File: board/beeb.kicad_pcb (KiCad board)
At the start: 2 copper layers, 24 parts, among them J2 AVR-JTAG-10, SW1 SW_DIP_x08, U2 ps2, U3 XC95144XL-TQ100, U4 beebKB, U5 OKI-78SR-3.3_1.5-W36-C

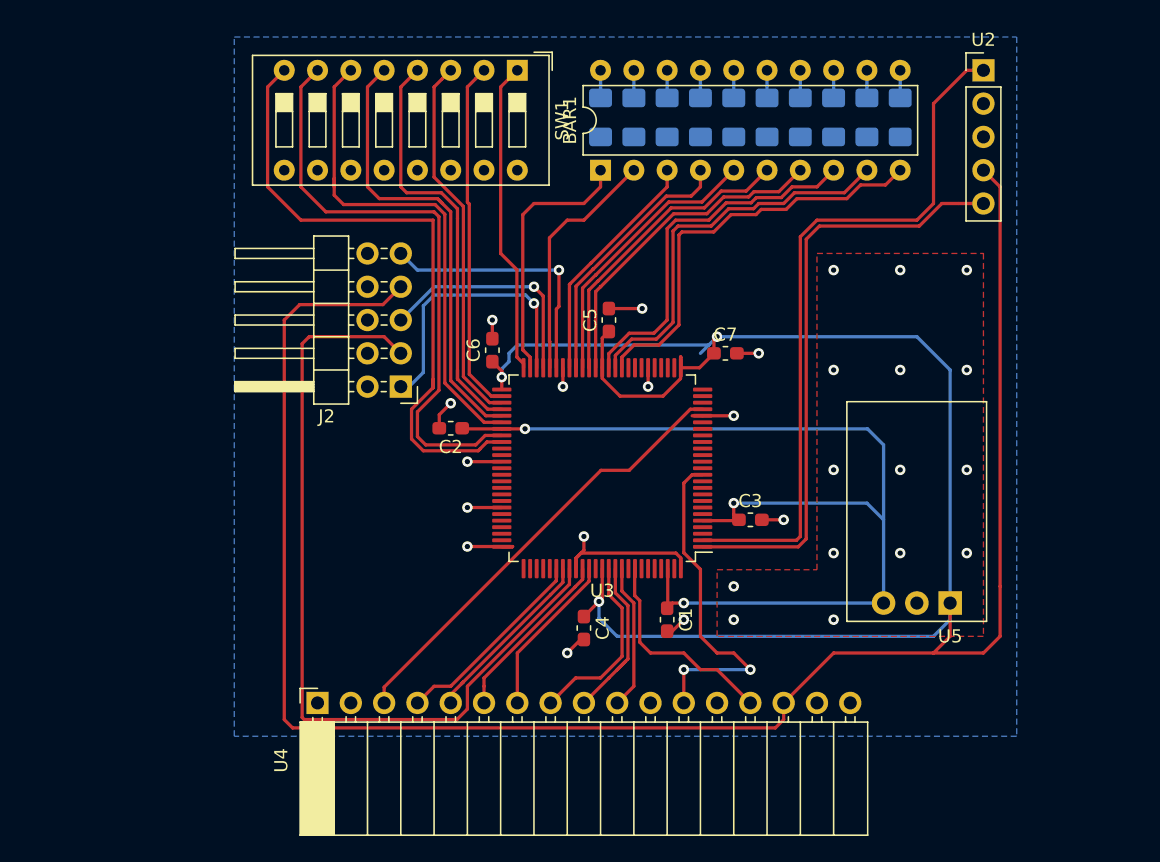
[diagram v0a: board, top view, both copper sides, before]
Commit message: Widen clearance around jtag vias
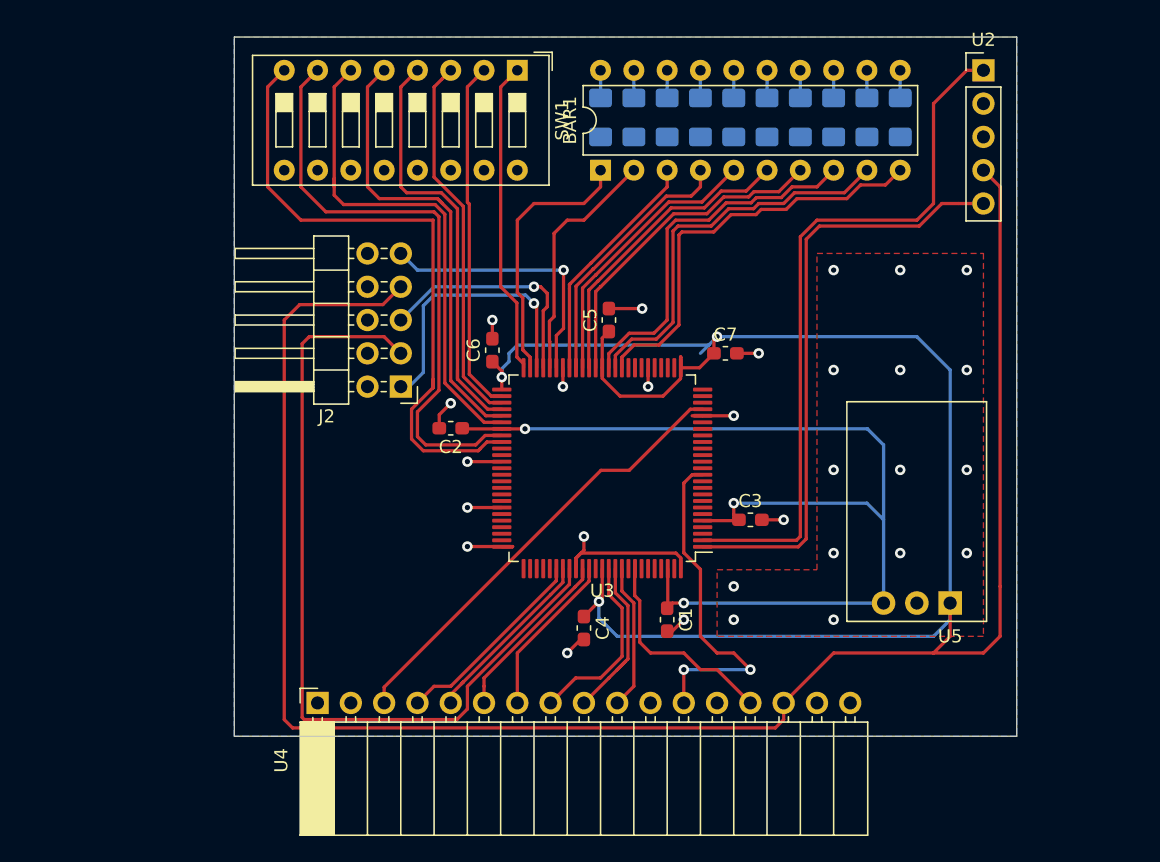
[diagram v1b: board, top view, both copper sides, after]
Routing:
- net /TMS: track 18.3 -> 18.9 mm
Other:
- board outline added: 59.7 x 53.3 mm
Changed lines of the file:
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@@
   (general
     (thickness 1.6)
-    (drawings 1)
-    (tracks 433)
+    (drawings 5)
+    (tracks 439)
     (zones 0)
     (modules 24)
@@
     (pad_to_mask_clearance 0.05)
     (aux_axis_origin 0 0)
+    (grid_origin 83.82 106.68)
     (visible_elements 7FFFFFFF)
     (pcbplotparams
@@
     )
   )
+  (gr_line (start 54.61 132.08) (end 54.61 78.74) (layer Edge.Cuts) (width 0.05))
+  (gr_line (start 114.3 132.08) (end 54.61 132.08) (layer Edge.Cuts) (width 0.05))
+  (gr_line (start 114.3 78.74) (end 114.3 132.08) (layer Edge.Cuts) (width 0.05))
+  (gr_line (start 54.61 78.74) (end 114.3 78.74) (layer Edge.Cuts) (width 0.05))
   (gr_poly (pts (xy 111.76 124.46) (xy 91.44 124.46) (xy 91.44 119.38) (xy 99.06 119.38) (xy 99.06 95.25) (xy 111.76 95.25)) (layer F.CrtYd) (width 0.1))
   (segment (start 82.55 81.28) (end 82.55 83.385) (width 0.25) (layer B.Cu) (net 1))
@@
   (via (at 110.49 118.11) (size 0.8) (drill 0.4) (layers F.Cu B.Cu) (net 11))
   (via (at 110.49 104.14) (size 0.8) (drill 0.4) (layers F.Cu B.Cu) (net 11))
-  (via (at 79.375 96.52) (size 0.8) (drill 0.4) (layers F.Cu B.Cu) (net 12))
-  (segment (start 79.375 99.299) (end 79.375 96.52) (width 0.25) (layer F.Cu) (net 12))
-  (segment (start 79.177 99.497) (end 79.375 99.299) (width 0.25) (layer F.Cu) (net 12))
-  (segment (start 79.177 103.9705) (end 79.177 99.497) (width 0.25) (layer F.Cu) (net 12))
+  (segment (start 79.177 103.9705) (end 79.177 101.51499) (width 0.25) (layer F.Cu) (net 12))
+  (segment (start 79.72699 100.965) (end 79.72699 96.52) (width 0.25) (layer F.Cu) (net 12))
+  (segment (start 79.177 101.51499) (end 79.72699 100.965) (width 0.25) (layer F.Cu) (net 12))
   (segment (start 68.58 96.52) (end 67.31 95.25) (width 0.25) (layer B.Cu) (net 12))
-  (segment (start 79.375 96.52) (end 68.58 96.52) (width 0.25) (layer B.Cu) (net 12))
+  (via (at 79.72699 96.52) (size 0.8) (drill 0.4) (layers F.Cu B.Cu) (net 12))
+  (segment (start 79.72699 96.52) (end 68.58 96.52) (width 0.25) (layer B.Cu) (net 12))
   (via (at 91.44 101.6) (size 0.8) (drill 0.4) (layers F.Cu B.Cu) (net 14))
   (segment (start 100.33 125.73) (end 96.52 129.54) (width 0.25) (layer F.Cu) (net 14))
@@
   (via (at 77.47 97.79) (size 0.8) (drill 0.4) (layers F.Cu B.Cu) (net 16))
   (segment (start 67.31 99.695) (end 67.31 100.33) (width 0.25) (layer B.Cu) (net 16))
-  (segment (start 78.177 98.497) (end 77.47 97.79) (width 0.25) (layer F.Cu) (net 16))
-  (segment (start 78.177 103.9705) (end 78.177 98.497) (width 0.25) (layer F.Cu) (net 16))
   (segment (start 67.31 100.32859) (end 67.31 100.33) (width 0.25) (layer B.Cu) (net 16))
   (segment (start 69.84859 97.79) (end 67.31 100.32859) (width 0.25) (layer B.Cu) (net 16))
   (segment (start 77.47 97.79) (end 69.84859 97.79) (width 0.25) (layer B.Cu) (net 16))
+  (segment (start 78.177 103.9705) (end 78.177 99.623) (width 0.25) (layer F.Cu) (net 16))
+  (segment (start 78.177 99.623) (end 78.486 99.314) (width 0.25) (layer F.Cu) (net 16))
+  (segment (start 77.978 97.79) (end 78.486 98.298) (width 0.25) (layer F.Cu) (net 16))
+  (segment (start 78.486 99.314) (end 78.486 98.298) (width 0.25) (layer F.Cu) (net 16))
+  (segment (start 77.978 97.79) (end 77.47 97.79) (width 0.25) (layer F.Cu) (net 16))
   (segment (start 66.04 101.6) (end 67.31 102.87) (width 0.25) (layer F.Cu) (net 18))
   (segment (start 60.325 101.6) (end 66.04 101.6) (width 0.25) (layer F.Cu) (net 18))
@@
   (segment (start 72.534999 91.475809) (end 72.39 91.33081) (width 0.25) (layer F.Cu) (net 26))
   (segment (start 72.39 91.33081) (end 72.39 82.55) (width 0.25) (layer F.Cu) (net 26))
+  (segment (start 76.677 103.663) (end 76.165989 103.151989) (width 0.25) (layer F.Cu) (net 27))
+  (segment (start 74.93 82.55) (end 76.2 81.28) (width 0.25) (layer F.Cu) (net 27))
+  (segment (start 76.165989 99.025989) (end 74.93 97.79) (width 0.25) (layer F.Cu) (net 27))
   (segment (start 76.677 103.9705) (end 76.677 103.663) (width 0.25) (layer F.Cu) (net 27))
-  (segment (start 76.677 103.663) (end 76.165989 103.151989) (width 0.25) (layer F.Cu) (net 27))
-  (segment (start 76.165989 103.151989) (end 76.165989 96.485989) (width 0.25) (layer F.Cu) (net 27))
-  (segment (start 74.93 95.25) (end 76.165989 96.485989) (width 0.25) (layer F.Cu) (net 27))
-  (segment (start 74.93 82.55) (end 74.93 95.25) (width 0.25) (layer F.Cu) (net 27))
-  (segment (start 74.93 82.55) (end 76.2 81.28) (width 0.25) (layer F.Cu) (net 27))
+  (segment (start 76.165989 103.151989) (end 76.165989 99.025989) (width 0.25) (layer F.Cu) (net 27))
+  (segment (start 74.93 97.79) (end 74.93 82.55) (width 0.25) (layer F.Cu) (net 27))
   (segment (start 76.2 125.73423) (end 76.2 129.54) (width 0.25) (layer F.Cu) (net 33))
   (segment (start 81.677 119.2955) (end 81.677 120.25723) (width 0.25) (layer F.Cu) (net 33))
@@
   (segment (start 87.63 88.9) (end 87.63 90.17282) (width 0.25) (layer F.Cu) (net 104))
   (segment (start 87.63 90.17282) (end 81.812859 95.989961) (width 0.25) (layer F.Cu) (net 104))
-  (segment (start 78.677 101.975002) (end 78.677 103.9705) (width 0.25) (layer F.Cu) (net 105))
-  (segment (start 78.649999 101.948001) (end 78.677 101.975002) (width 0.25) (layer F.Cu) (net 105))
-  (segment (start 78.649999 98.507951) (end 78.649999 101.948001) (width 0.25) (layer F.Cu) (net 105))
-  (segment (start 85.09 88.9) (end 81.28 92.71) (width 0.25) (layer F.Cu) (net 105))
-  (segment (start 80.01 92.71) (end 78.649999 94.070001) (width 0.25) (layer F.Cu) (net 105))
-  (segment (start 81.28 92.71) (end 80.01 92.71) (width 0.25) (layer F.Cu) (net 105))
-  (segment (start 78.649999 98.507951) (end 78.649999 94.070001) (width 0.25) (layer F.Cu) (net 105))
-  (segment (start 82.55 90.17) (end 82.55 88.9) (width 0.25) (layer F.Cu) (net 106))
-  (segment (start 77.177 103.9705) (end 77.177 103.167298) (width 0.25) (layer F.Cu) (net 106))
-  (segment (start 77.47 91.44) (end 81.28 91.44) (width 0.25) (layer F.Cu) (net 106))
-  (segment (start 81.28 91.44) (end 82.55 90.17) (width 0.25) (layer F.Cu) (net 106))
-  (segment (start 77.177 103.167298) (end 76.615999 102.606297) (width 0.25) (layer F.Cu) (net 106))
-  (segment (start 76.615999 102.606297) (end 76.615999 92.294001) (width 0.25) (layer F.Cu) (net 106))
-  (segment (start 76.615999 92.294001) (end 77.47 91.44) (width 0.25) (layer F.Cu) (net 106))
+  (segment (start 81.28 92.71) (end 85.09 88.9) (width 0.25) (layer F.Cu) (net 105))
+  (segment (start 80.01 92.71) (end 81.28 92.71) (width 0.25) (layer F.Cu) (net 105))
+  (segment (start 79.001989 93.718011) (end 80.01 92.71) (width 0.25) (layer F.Cu) (net 105))
+  (segment (start 78.677 103.9705) (end 78.677 101.975002) (width 0.25) (layer F.Cu) (net 105))
+  (segment (start 78.677 101.975002) (end 78.649999 101.948001) (width 0.25) (layer F.Cu) (net 105))
+  (segment (start 78.649999 101.948001) (end 78.649999 100.420001) (width 0.25) (layer F.Cu) (net 105))
+  (segment (start 78.649999 100.420001) (end 79.001989 100.068011) (width 0.25) (layer F.Cu) (net 105))
+  (segment (start 79.001989 100.068011) (end 79.001989 93.718011) (width 0.25) (layer F.Cu) (net 105))
+  (segment (start 76.615999 98.644001) (end 76.615999 102.606297) (width 0.25) (layer F.Cu) (net 106))
+  (segment (start 82.55 88.9) (end 82.55 90.17) (width 0.25) (layer F.Cu) (net 106))
+  (segment (start 77.177 103.167298) (end 77.177 103.9705) (width 0.25) (layer F.Cu) (net 106))
+  (segment (start 82.55 90.17) (end 81.28 91.44) (width 0.25) (layer F.Cu) (net 106))
+  (segment (start 76.615999 102.606297) (end 77.177 103.167298) (width 0.25) (layer F.Cu) (net 106))
+  (segment (start 81.28 91.44) (end 77.47 91.44) (width 0.25) (layer F.Cu) (net 106))
+  (segment (start 76.2 98.228002) (end 76.615999 98.644001) (width 0.25) (layer F.Cu) (net 106))
+  (segment (start 77.47 91.44) (end 76.2 92.71) (width 0.25) (layer F.Cu) (net 106))
+  (segment (start 76.2 92.71) (end 76.2 98.228002) (width 0.25) (layer F.Cu) (net 106))
   (zone (net 11) (net_name GND) (layer B.Cu) (hatch edge 0.508)
     (connect_pads (clearance 0.508))
     (min_thickness 0.254)
-    (fill (arc_segments 32) (thermal_gap 0.508) (thermal_bridge_width 0.508))
+    (fill yes (arc_segments 32) (thermal_gap 0.508) (thermal_bridge_width 0.508))
     (polygon
       (pts
@@
     (connect_pads (clearance 0.508))
     (min_thickness 0.254)
-    (fill (arc_segments 32) (thermal_gap 0.508) (thermal_bridge_width 0.508))
+    (fill yes (arc_segments 32) (thermal_gap 0.508) (thermal_bridge_width 0.508))
     (polygon
       (pts

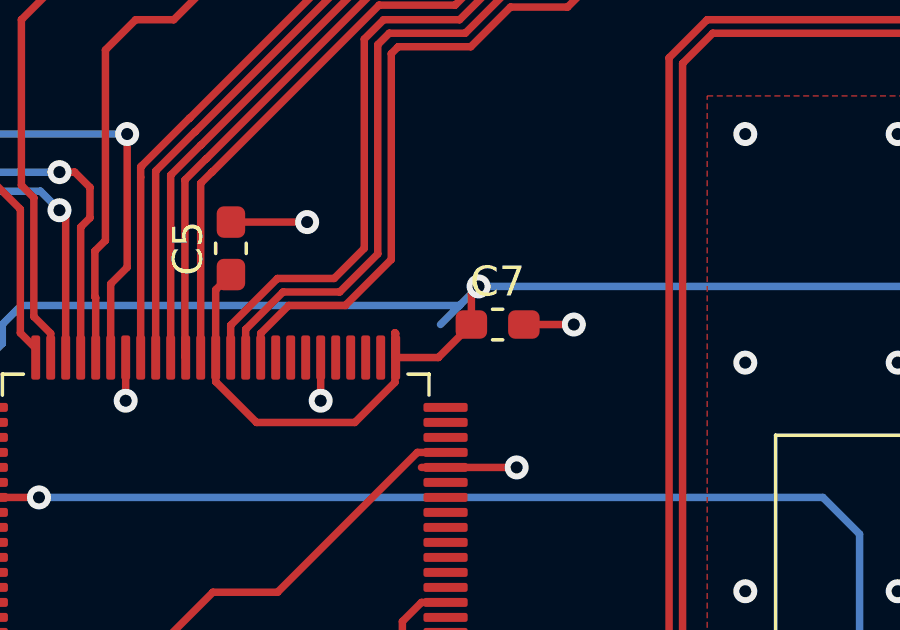
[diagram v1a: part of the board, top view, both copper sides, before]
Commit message: remove spur trace
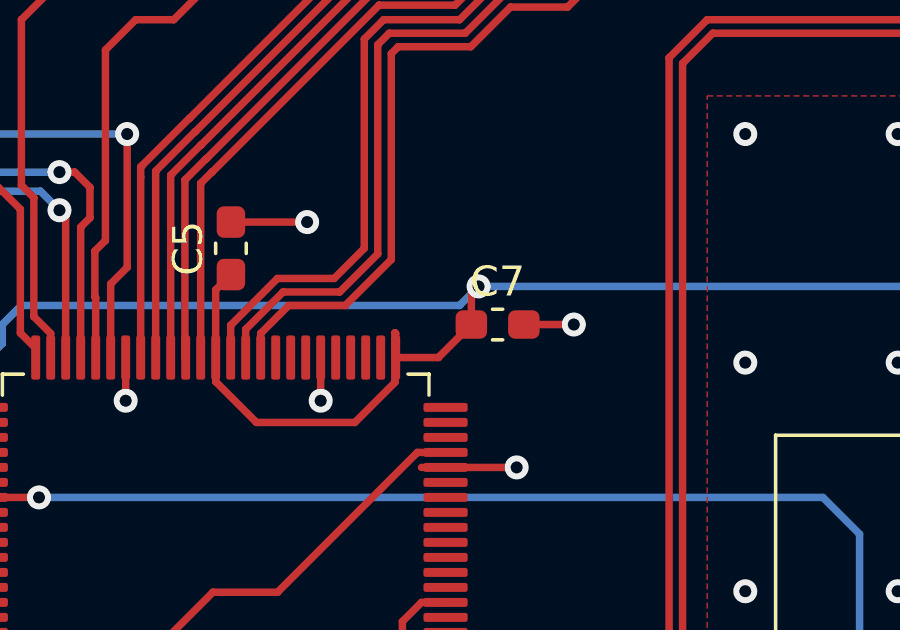
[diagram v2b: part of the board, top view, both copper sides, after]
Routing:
- net +5V: track 250.1 -> 249.2 mm
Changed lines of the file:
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@@
     (thickness 1.6)
     (drawings 5)
-    (tracks 439)
+    (tracks 438)
     (zones 0)
     (modules 24)
@@
   (segment (start 91.2 101.84) (end 91.44 101.6) (width 0.25) (layer F.Cu) (net 14))
   (segment (start 91.2 102.87) (end 91.2 101.84) (width 0.25) (layer F.Cu) (net 14))
-  (segment (start 90.805 102.235) (end 90.17 102.87) (width 0.25) (layer B.Cu) (net 14))
   (segment (start 91.44 101.6) (end 90.805 102.235) (width 0.25) (layer B.Cu) (net 14))
   (segment (start 75.0145 104.6905) (end 75.0145 104.2245) (width 0.25) (layer F.Cu) (net 14))
